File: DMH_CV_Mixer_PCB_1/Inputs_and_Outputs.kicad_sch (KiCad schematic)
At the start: 7 parts, among them J1 TS_Jack_6.35mm_Sw, J2 TS_Jack_6.35mm_Sw, J200 IDC_02x05, J3 TS_Jack_6.35mm_Sw, J4 TS_Jack_6.35mm_Sw, J50 Conn_01x06, J60 Conn_01x06

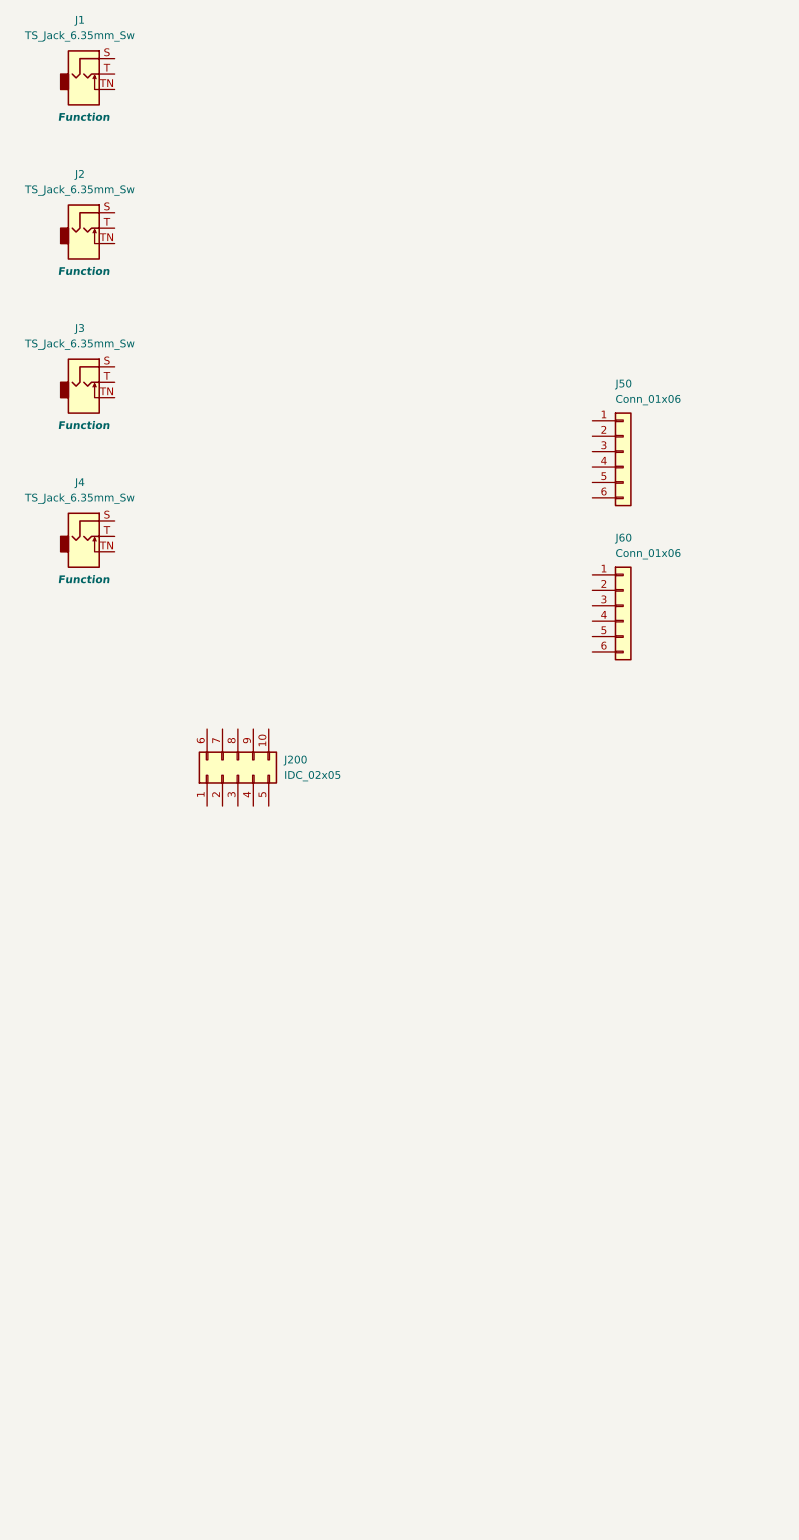
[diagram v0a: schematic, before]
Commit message: Started IO part design
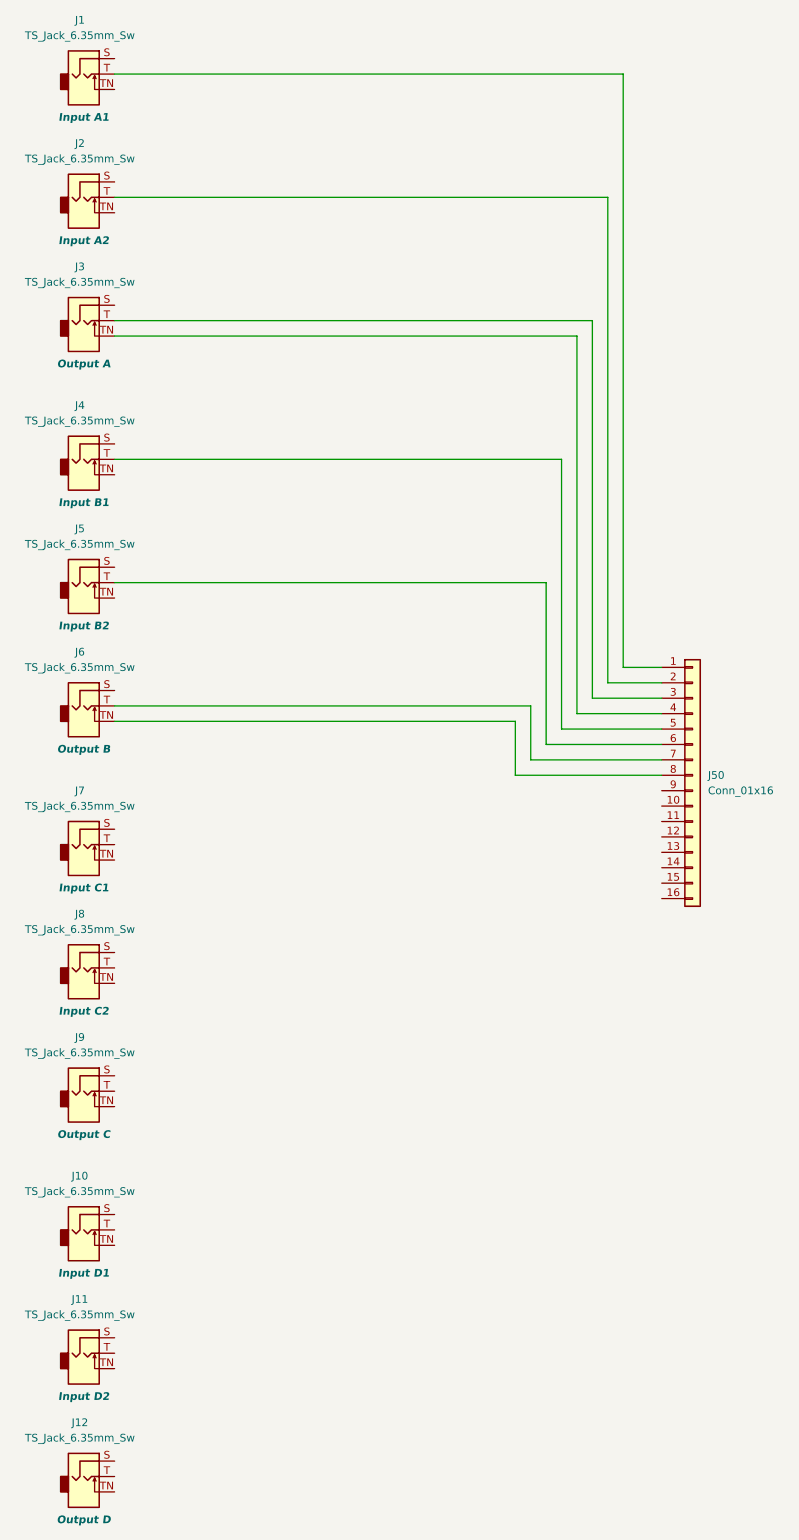
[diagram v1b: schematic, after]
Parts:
- removed J200: IDC_02x05, SynthStuff:IDC-Header_2x05_P2.54mm_Vertical_BackBone, symbol SynthStuff:BackBone_Connector_10Pin
- removed J50, J60: Conn_01x06, Connector_PinSocket_2.54mm:PinSocket_1x06_P2.54mm_Vertical, symbol Connector_Generic:Conn_01x06
- added J10, J11, J12, J5, J6, J7, J8, J9: TS_Jack_6.35mm_Sw, SynthStuff:CUI_MJ-63052A, symbol SynthStuff:TS_Jack_6.35mm_Sw
- added J50: Conn_01x16, Connector_PinHeader_2.54mm:PinHeader_1x16_P2.54mm_Vertical, symbol Connector_Generic:Conn_01x16
- J1: Function Function -> Input A1
- J2: Function Function -> Input A2
- J3: Function Function -> Output A
- J4: Function Function -> Input B1
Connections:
- net at J3.T: now also J50.3 (Pin_3)
- net at J3.TN: now also J50.4 (Pin_4)
- net at J4.T: now also J50.5 (Pin_5)
- net at J1.T: now also J50.1 (Pin_1)
- net at J2.T: now also J50.2 (Pin_2)
- new net: J5.T, J50.6 (Pin_6)
- new net: J50.7 (Pin_7), J6.T
- new net: J50.8 (Pin_8), J6.TN
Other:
- moved on the sheet: J2, J3
